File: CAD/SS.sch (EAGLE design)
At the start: 132 parts, among them Q1 SN74AHC-NOR, Q2 UMD5N, Q3 MIC5205, Q4 SN74AHC-AND, Q5 BFP460, Q6 TCR1HF50, T1 MMBTRA104SS, X1 ANTENNA, X2 RADIO, X3 INP, X4 AMP-O, X5 BPF-O

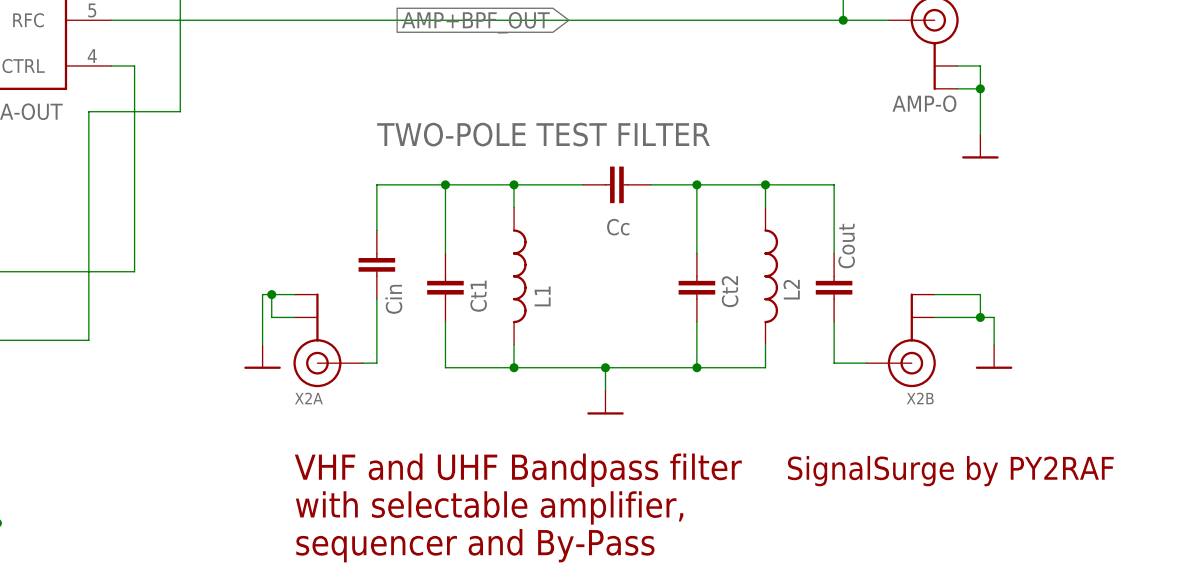
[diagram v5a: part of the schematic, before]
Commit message: Added another series capacitor in 2 pole test filter
The two-pole filter, used to tune/test/evaluate UHF filters sometimes
requires a very small capacitance value. Adding a second serial coupling
cap in case of need to put them in series to reduce capacitance and yield
a lower value. Otherwise, jumper it with a 0 ohm chip resistor/jumper.
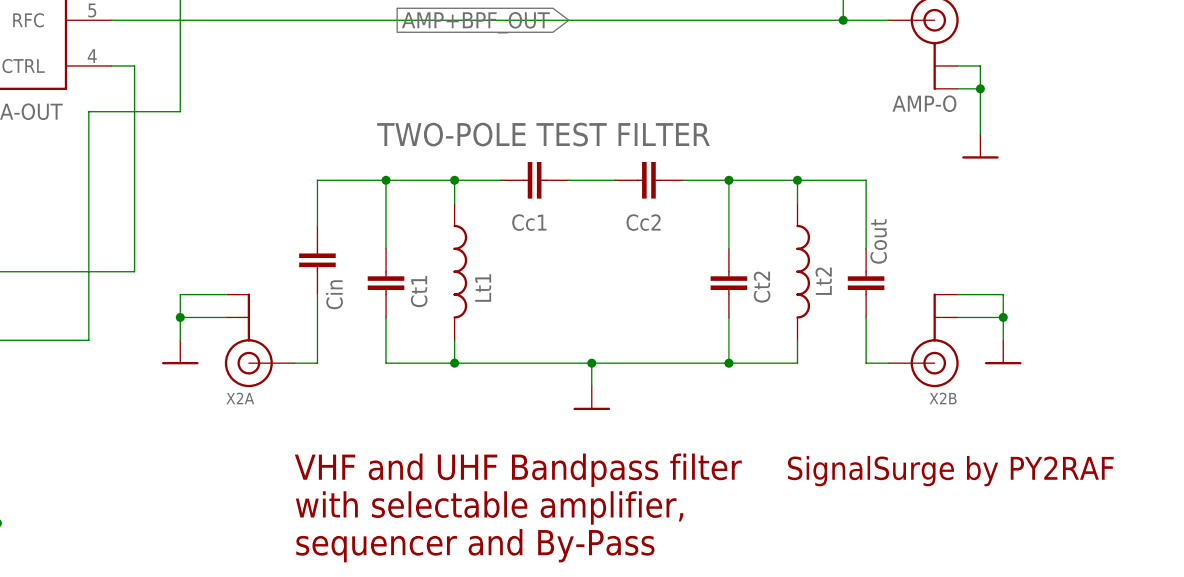
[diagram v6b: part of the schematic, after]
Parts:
- added L18: Cc1, aarf:C-0805
- L13: value Cc -> Cc2
- L16: value L1 -> Lt1
- L17: value L2 -> Lt2
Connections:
- net T-V-IN renamed N$11
- net T-V-OUT renamed N$6
- new net N$5: L13.1, L18.2
- net T-V-P1: now also L18.1; no longer L13.1
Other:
- moved on the sheet: X2A, X2B
